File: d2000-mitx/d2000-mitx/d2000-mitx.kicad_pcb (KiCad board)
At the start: 2 copper layers, 8.8 x 7.6 mm, 0 parts

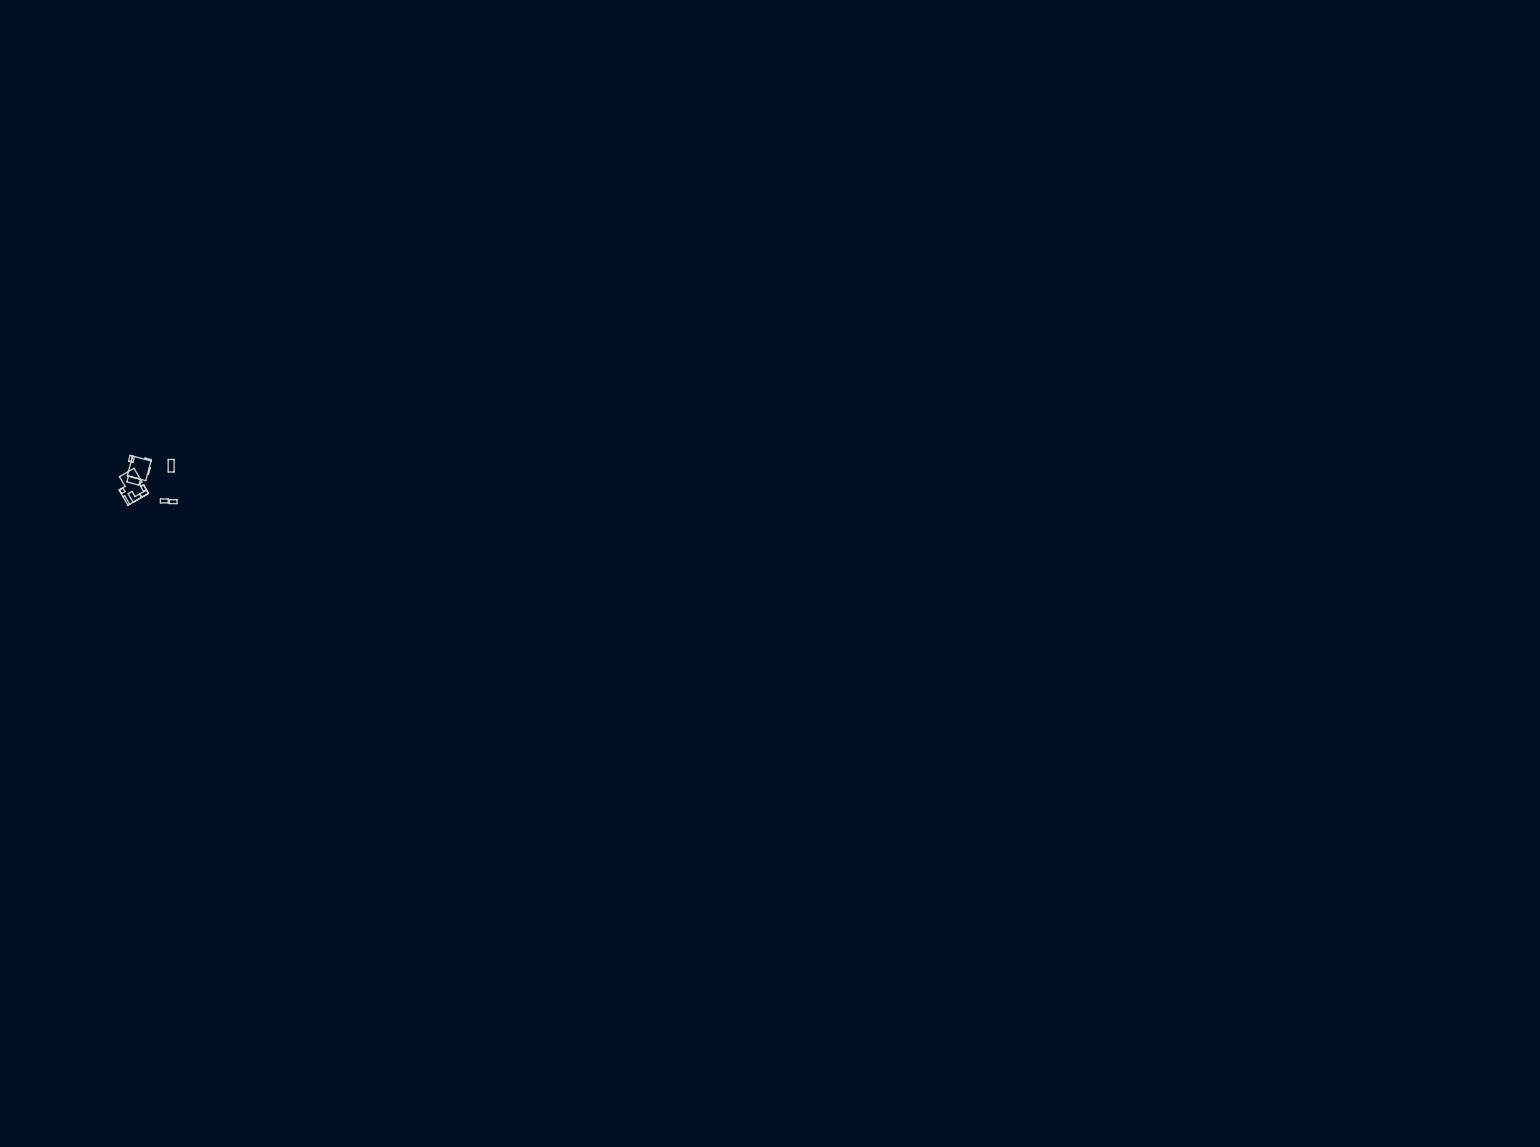
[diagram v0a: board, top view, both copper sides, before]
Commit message: d2000-mitx: add d2000 footprint
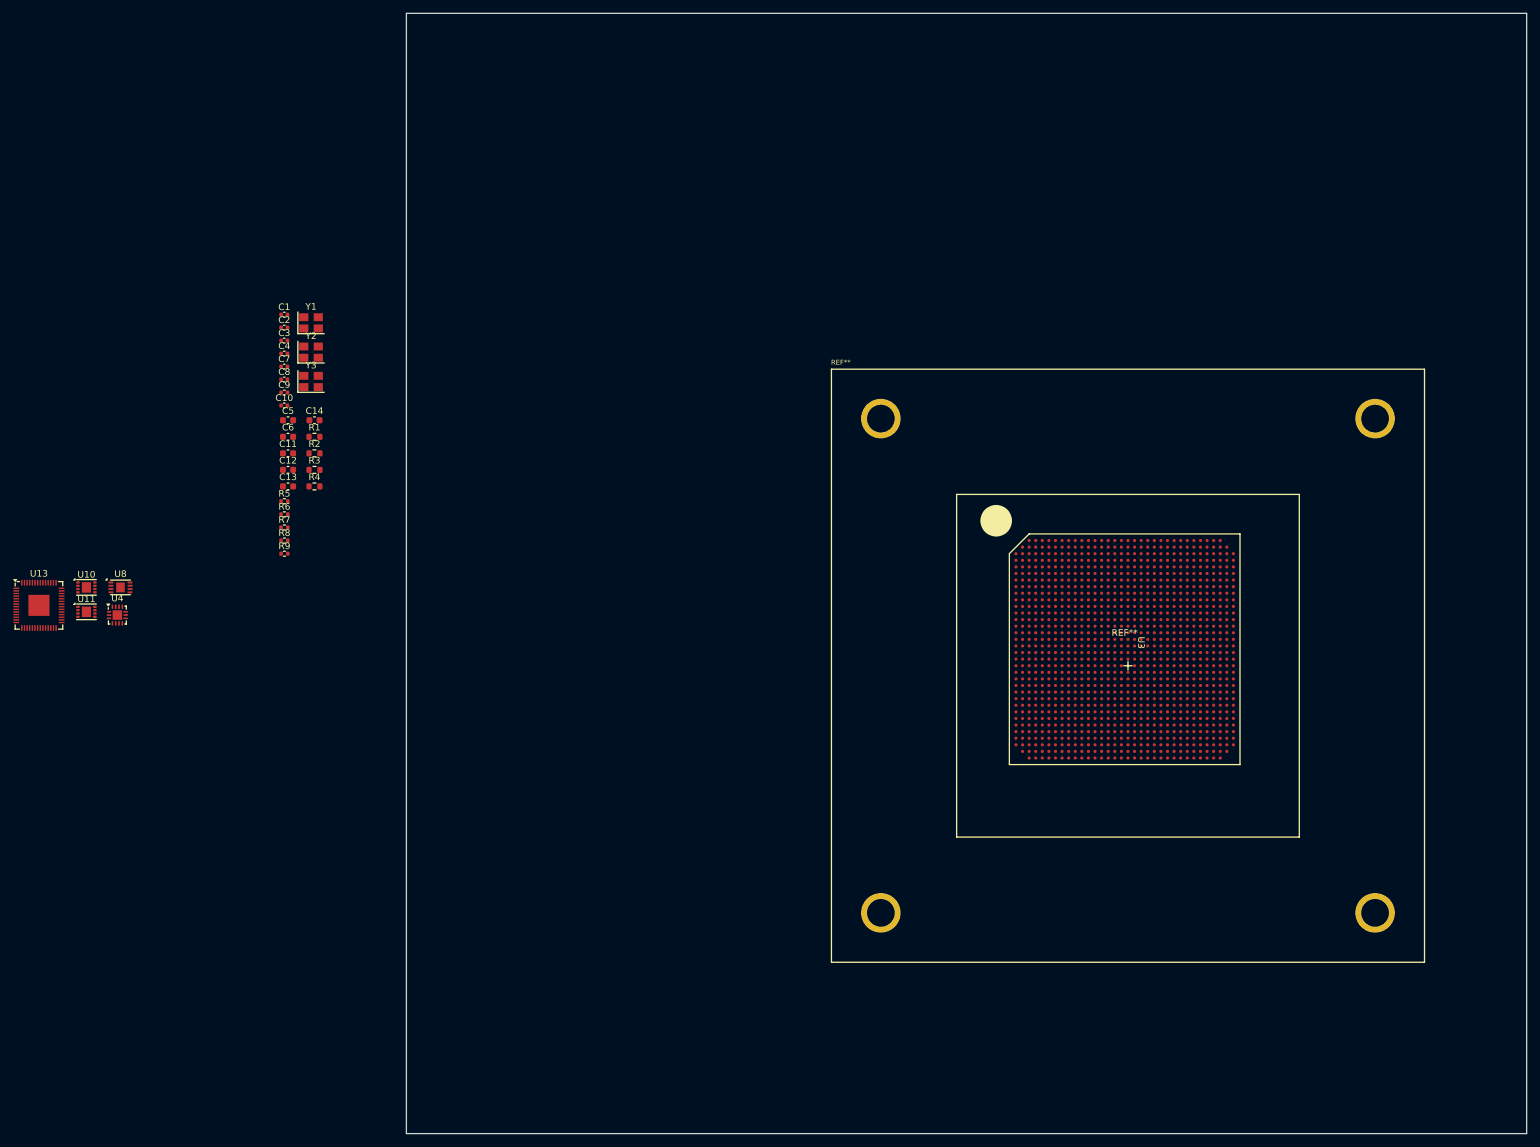
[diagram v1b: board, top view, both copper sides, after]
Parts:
- added C1: 100n, Capacitor_SMD:C_0402_1005Metric, F.Cu at (73.0, 58.2)
- added C10: 10uF, Capacitor_SMD:C_0402_1005Metric, F.Cu at (73.0, 72.0)
- added C11: 22pF, Capacitor_SMD:C_0603_1608Metric, F.Cu at (73.5, 79.3)
- added C12: 22pF, Capacitor_SMD:C_0603_1608Metric, F.Cu at (73.5, 81.8)
- added C13: 22pF, Capacitor_SMD:C_0603_1608Metric, F.Cu at (73.5, 84.3)
- added C14: 22pF, Capacitor_SMD:C_0603_1608Metric, F.Cu at (77.5, 74.2)
- added C2: 100n, Capacitor_SMD:C_0402_1005Metric, F.Cu at (73.0, 60.2)
- added C3: 10uF, Capacitor_SMD:C_0402_1005Metric, F.Cu at (73.0, 62.2)
- added C4: 10uF, Capacitor_SMD:C_0402_1005Metric, F.Cu at (73.0, 64.1)
- added C5: 22pF, Capacitor_SMD:C_0603_1608Metric, F.Cu at (73.5, 74.2)
- added C6: 22pF, Capacitor_SMD:C_0603_1608Metric, F.Cu at (73.5, 76.8)
- added C7: 100n, Capacitor_SMD:C_0402_1005Metric, F.Cu at (73.0, 66.1)
- added C8: 100n, Capacitor_SMD:C_0402_1005Metric, F.Cu at (73.0, 68.1)
- added C9: 10uF, Capacitor_SMD:C_0402_1005Metric, F.Cu at (73.0, 70.0)
- added R1: 6.04k, Resistor_SMD:R_0603_1608Metric, F.Cu at (77.5, 76.8)
- added R2: 15k, Resistor_SMD:R_0603_1608Metric, F.Cu at (77.5, 79.3)
- added R3: 6.04k, Resistor_SMD:R_0603_1608Metric, F.Cu at (77.5, 81.8)
- added R4: 15k, Resistor_SMD:R_0603_1608Metric, F.Cu at (77.5, 84.3)
- added R5: 10K, Resistor_SMD:R_0402_1005Metric, F.Cu at (73.0, 86.5)
- added R6: 1K, Resistor_SMD:R_0402_1005Metric, F.Cu at (73.0, 88.5)
- added R7: 22R, Resistor_SMD:R_0402_1005Metric, F.Cu at (73.0, 90.5)
- added R8: 22R, Resistor_SMD:R_0402_1005Metric, F.Cu at (73.0, 92.5)
- added R9: 1K, Resistor_SMD:R_0402_1005Metric, F.Cu at (73.0, 94.5)
- added REF**: FANSOCKET_4N_FANSOCKET9000X9000, FanSocket:FANSOCKET_4N_FANSOCKET9000X9000, F.Cu at (200.5, 107.0)
- added U10: TPS784105QWDRBRQ1, Package_SON:SON-8-1EP_3x2mm_P0.5mm_EP1.4x1.6mm, F.Cu at (42.9, 99.6)
- added U11: TPS784105QWDRBRQ1, Package_SON:SON-8-1EP_3x2mm_P0.5mm_EP1.4x1.6mm, F.Cu at (42.9, 103.3)
- added U13: RP2040, Package_DFN_QFN:QFN-56-1EP_7x7mm_P0.4mm_EP3.2x3.2mm, F.Cu at (35.7, 102.3)
- added U3: ~, D2000:D2000_DDR4_BGA1144P100_3500X350, F.Cu at (202.5, 108.0)
- added U4: FUSB302B01MPX, Package_DFN_QFN:WQFN-14-1EP_2.5x2.5mm_P0.5mm_EP1.45x1.45mm, F.Cu at (47.6, 103.8)
- added U8: W25Q32JVSS, Package_DFN_QFN:DFN-8-1EP_3x2mm_P0.5mm_EP1.3x1.5mm, F.Cu at (48.1, 99.6)
- added Y1: Crystal_GND23, Crystal:Crystal_SMD_3225-4Pin_3.2x2.5mm, F.Cu at (77.0, 59.5)
- added Y2: Crystal_GND23, Crystal:Crystal_SMD_3225-4Pin_3.2x2.5mm, F.Cu at (77.0, 63.9)
- added Y3: 12MHz, Crystal:Crystal_SMD_3225-4Pin_3.2x2.5mm, F.Cu at (77.0, 68.4)
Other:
- board size 8.8 x 7.6 mm -> 170 x 170 mm
- copper layers 2 -> 6
- board text removed: "2.9"
- board text removed: "3.1"
- board text removed: "bed"
- board text removed: "desk (curved)"
- board text removed: "desk (ikea)"
- board text removed: "door"
- board text removed: "server rack"
- board text removed: "server rack in cupboard"
- board text removed: "window/door"
- board text removed: "workbench"

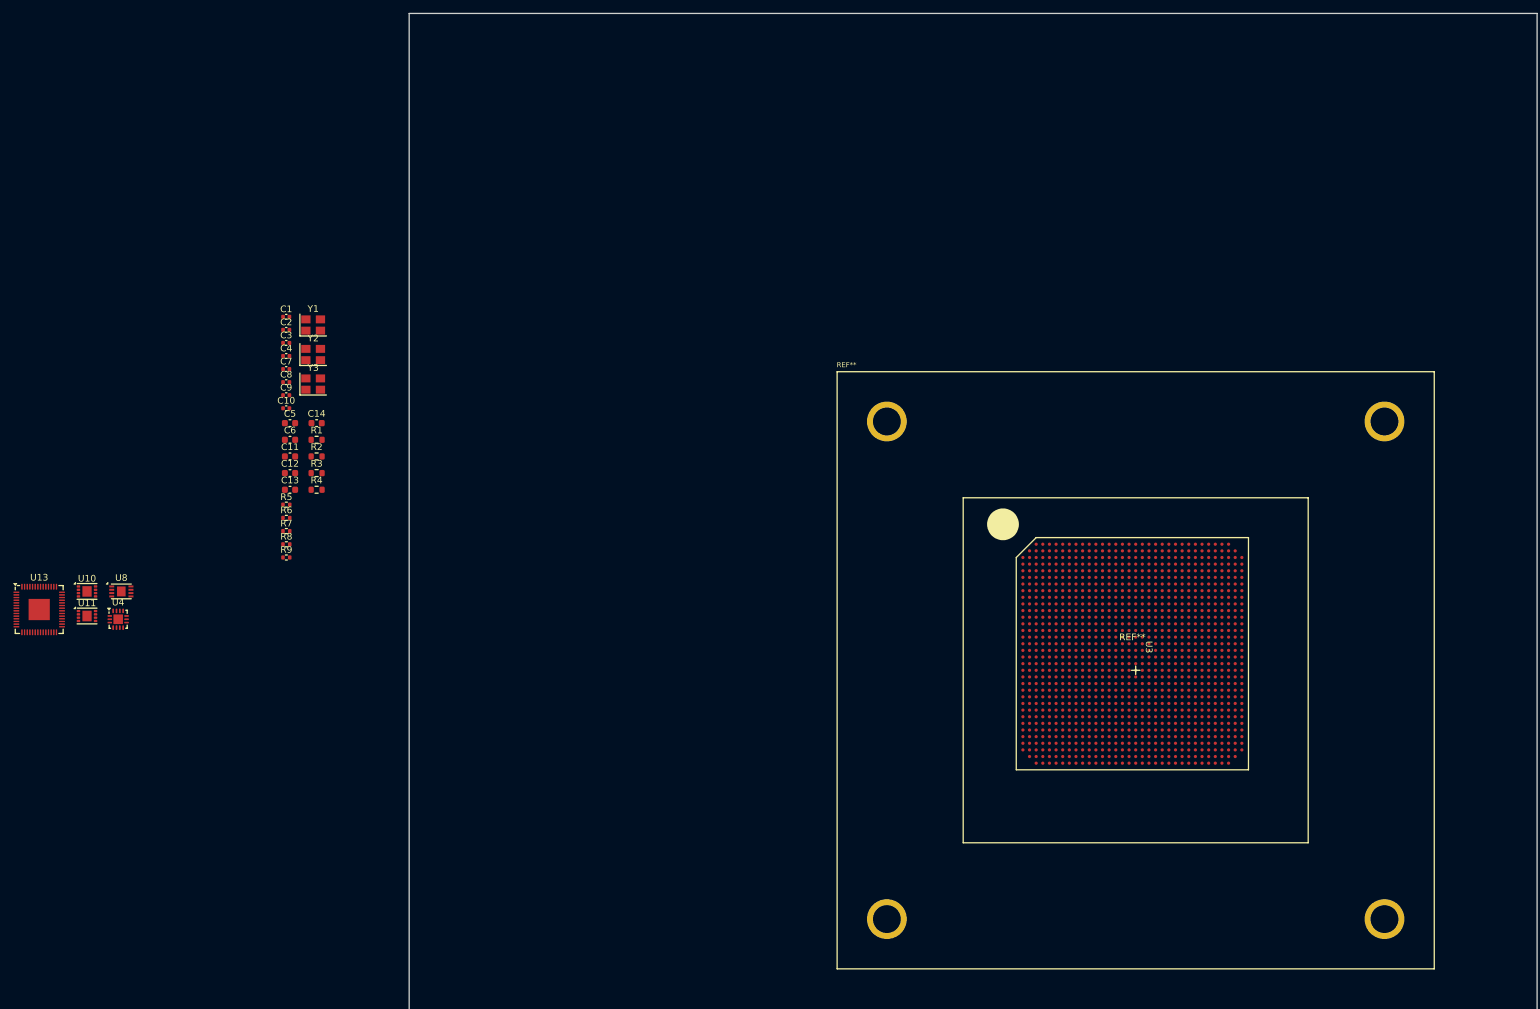
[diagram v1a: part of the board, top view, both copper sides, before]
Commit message: d2000-mitx: slight schem tweaks, rough board placements
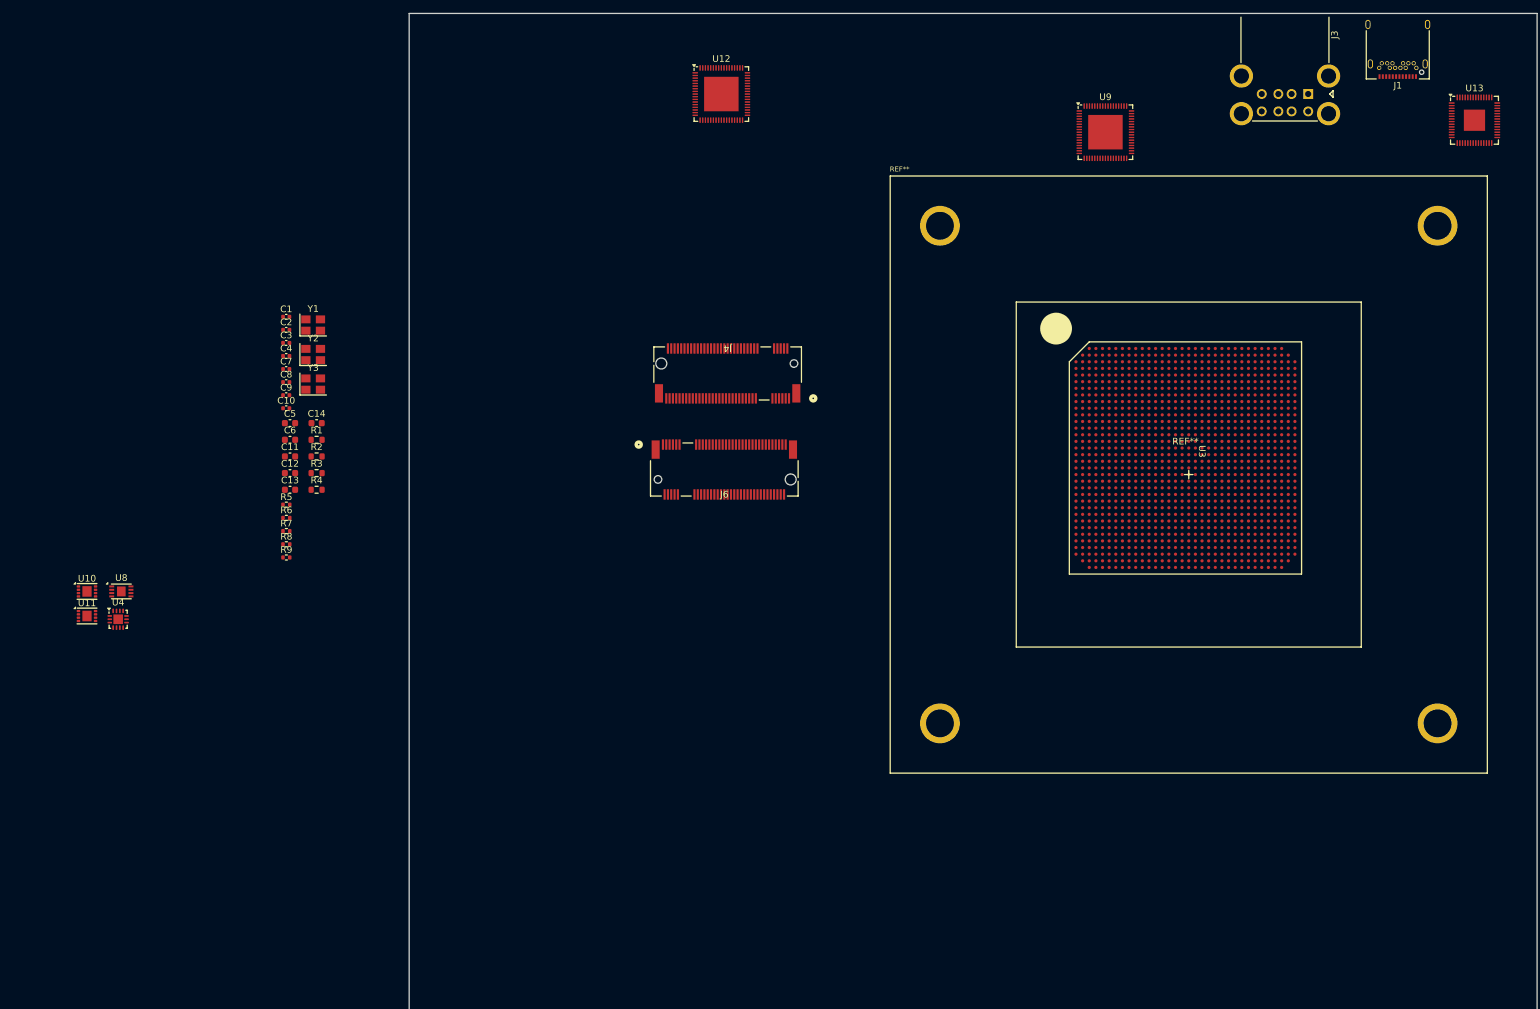
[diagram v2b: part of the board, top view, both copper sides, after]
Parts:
- added J1: USB 3.1 + PD INPUT, Connector_USB:USB_C_Receptacle_Amphenol_12401548E4-2A, F.Cu at (240.5, 17.0)
- added J3: USB3_A_Stacked, Connector_USB:USB_A_CUI_UJ2-ADH-TH_Horizontal_Stacked, F.Cu at (227.0, 24.6)
- added J4: M.2_NVME, 2199119-3-M.2:CONN75_2199119-3_TEC, F.Cu at (139.5, 66.8)
- added J6: M.2_WIFI, 2199119-3-M.2:CONN75_2199119-3_TEC, F.Cu at (139.0, 81.2)
- added U12: VL805 REAR I/O, Package_DFN_QFN:QFN-68-1EP_8x8mm_P0.4mm_EP5.2x5.2mm, F.Cu at (138.6, 24.6)
- added U9: VL805 REAR I/O, Package_DFN_QFN:QFN-68-1EP_8x8mm_P0.4mm_EP5.2x5.2mm, F.Cu at (196.4, 30.4)
- moved U13 228.5 mm to (252.1, 28.6)
- moved REF** 30.6 mm to (208.5, 77.5)
- moved U3 30.6 mm to (210.5, 78.5)
